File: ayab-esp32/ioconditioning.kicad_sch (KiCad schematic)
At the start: 41 parts, among them U702 LM393, U703 LM393

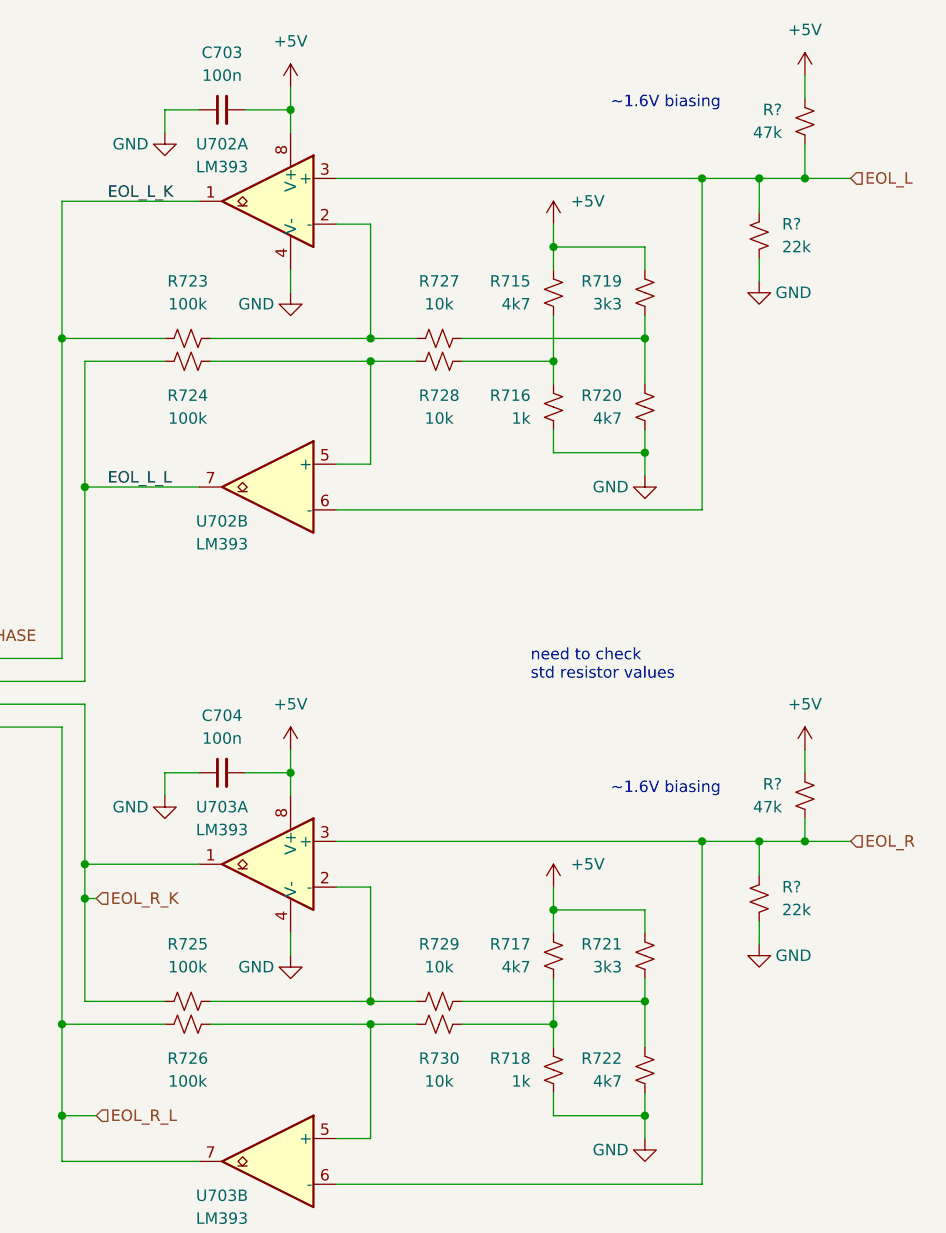
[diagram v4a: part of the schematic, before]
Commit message: refactor for i2c expander
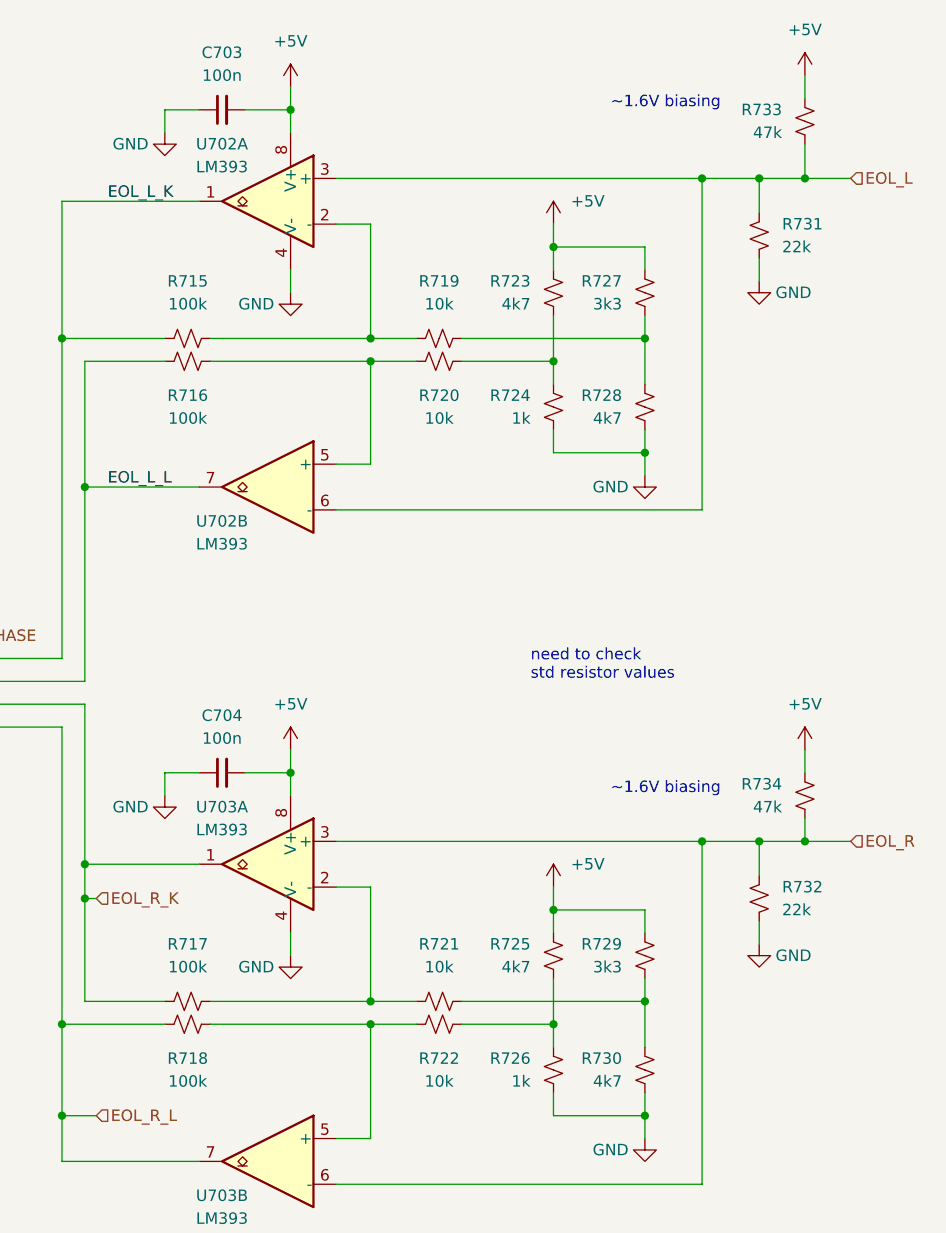
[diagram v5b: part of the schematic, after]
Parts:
- gave numbers to parts that had none: 4
- renumbered R723 to R715, R724 to R716, R725 to R717, R726 to R718, R727 to R719, R728 to R720, R729 to R721, R730 to R722, R715 to R723, R716 to R724, R717 to R725, R718 to R726, R719 to R727, R720 to R728, R721 to R729, R722 to R730

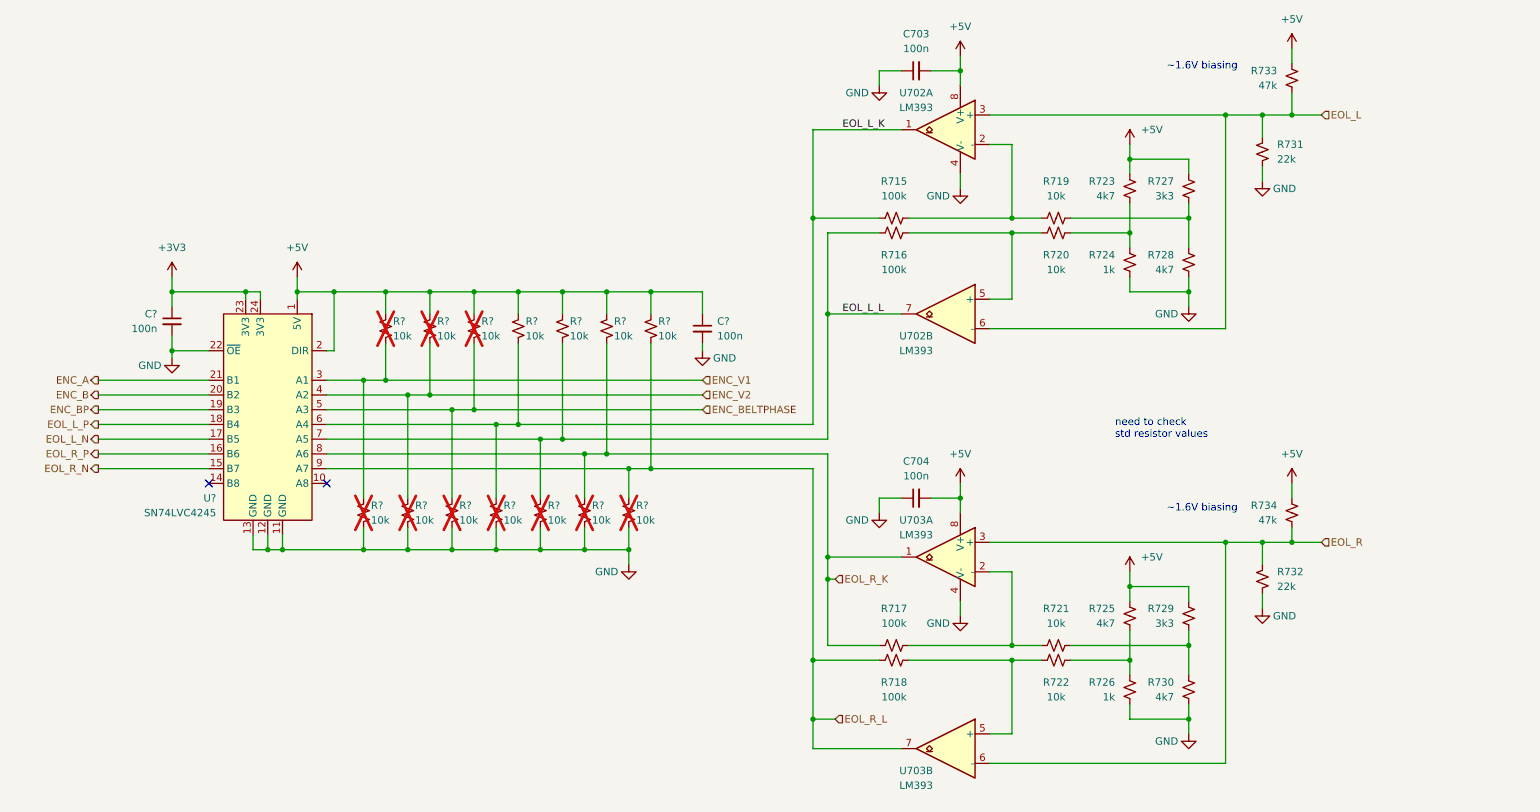
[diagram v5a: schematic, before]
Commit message: add component selection, bom
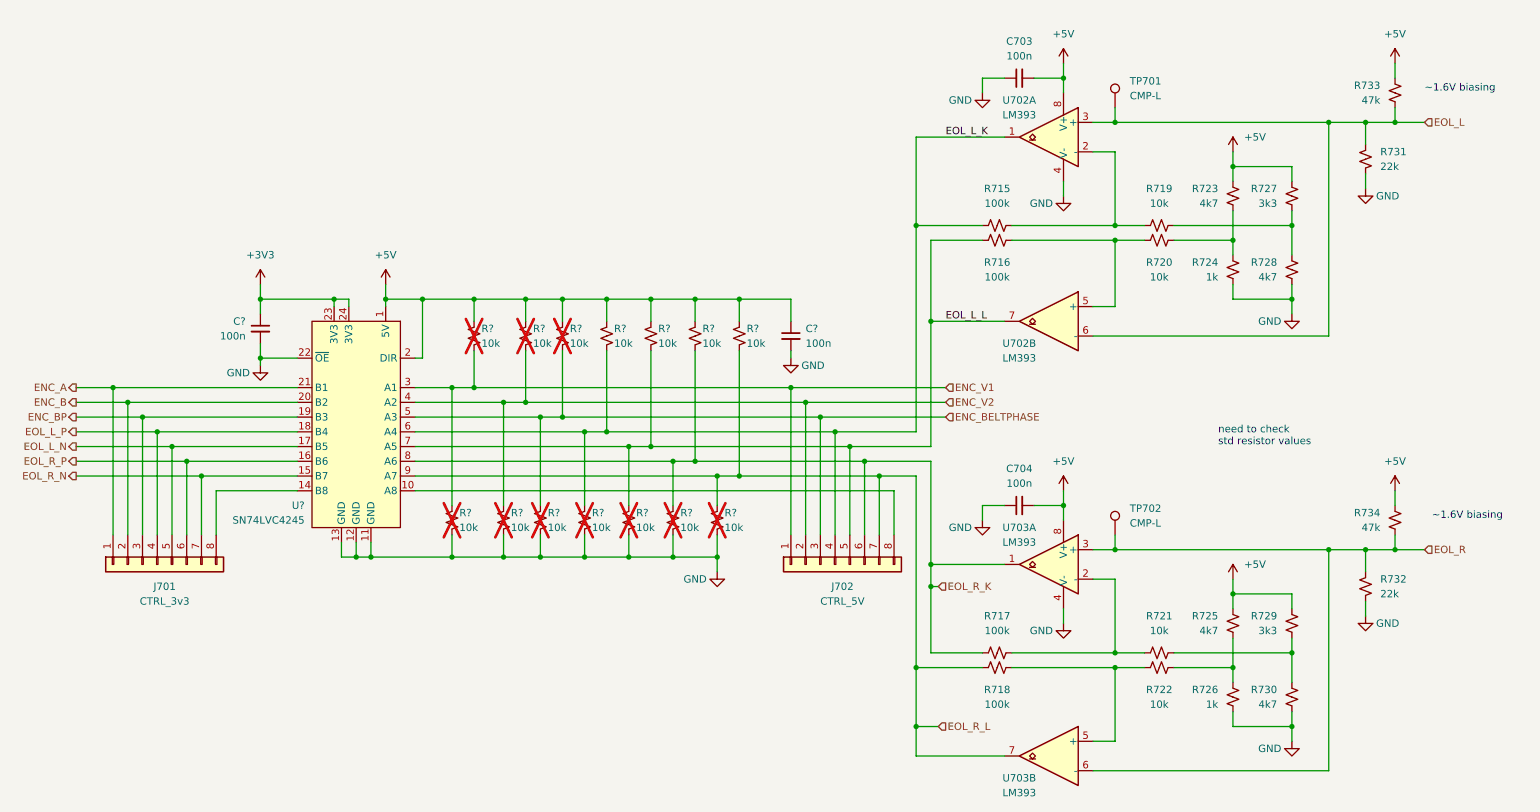
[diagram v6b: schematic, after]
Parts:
- added J701: CTRL_3v3, Connector_PinSocket_2.54mm:PinSocket_2x04_P2.54mm_Vertical, symbol Library:Conn_01x08
- added J702: CTRL_5V, Connector_PinSocket_2.54mm:PinSocket_2x04_P2.54mm_Vertical, symbol Library:Conn_01x08
- added TP701, TP702: CMP-L, TestPoint:TestPoint_Pad_D2.0mm, symbol Library:TestPoint
- C703, C704, C? (x2): footprint (none) -> Capacitor_SMD:C_0603_1608Metric; symbol ayab-esp32:C_Small -> Library:C_Small; LCSC ID (none) -> C57112; OEM (none) -> FH (Guangdong Fenghua Advanced Tech); OEM PN (none) -> 0603B103K500NT; Package (none) -> 0603; Voltage rating (none) -> 24V X7R
- R715, R716, R717, R718: footprint (none) -> Resistor_SMD:R_0603_1608Metric; symbol ayab-esp32:R_Small_US -> Library:R_Small_US; LCSC ID (none) -> C25803; OEM (none) -> UNI-ROYAL(Uniroyal Elec); OEM PN (none) -> 0603WAF1003T5E; Package (none) -> 0603
- R719, R720, R721, R722, R? (x14): footprint (none) -> Resistor_SMD:R_0603_1608Metric; symbol ayab-esp32:R_Small_US -> Library:R_Small_US; LCSC ID (none) -> C25804; OEM (none) -> UNI-ROYAL(Uniroyal Elec); OEM PN (none) -> 0603WAF1002T5E; Package (none) -> 0603
- R723, R725, R728, R730: footprint (none) -> Resistor_SMD:R_0603_1608Metric; symbol ayab-esp32:R_Small_US -> Library:R_Small_US; LCSC ID (none) -> C23162; OEM (none) -> UNI-ROYAL(Uniroyal Elec); OEM PN (none) -> 0603WAF4701T5E; Package (none) -> 0603
- R724, R726: footprint (none) -> Resistor_SMD:R_0603_1608Metric; symbol ayab-esp32:R_Small_US -> Library:R_Small_US; LCSC ID (none) -> C21190; OEM (none) -> UNI-ROYAL(Uniroyal Elec); OEM PN (none) -> 0603WAF1001T5E; Package (none) -> 0603
- R727, R729: footprint (none) -> Resistor_SMD:R_0603_1608Metric; symbol ayab-esp32:R_Small_US -> Library:R_Small_US; LCSC ID (none) -> C22978; OEM (none) -> UNI-ROYAL(Uniroyal Elec); OEM PN (none) -> 0603WAF3301T5E; Package (none) -> 0603
- R731, R732: footprint (none) -> Resistor_SMD:R_0603_1608Metric; symbol ayab-esp32:R_Small_US -> Library:R_Small_US; LCSC ID (none) -> C31850; OEM (none) -> UNI-ROYAL(Uniroyal Elec); OEM PN (none) -> 0603WAF2202T5E; Package (none) -> 0603
- R733, R734: footprint (none) -> Resistor_SMD:R_0603_1608Metric; symbol ayab-esp32:R_Small_US -> Library:R_Small_US; LCSC ID (none) -> C25819; OEM (none) -> UNI-ROYAL(Uniroyal Elec); OEM PN (none) -> 0603WAF4702T5E; Package (none) -> 0603
- U702, U703: footprint (none) -> Package_SO:SOIC-8_3.9x4.9mm_P1.27mm; symbol ayab-esp32:LM393 -> Library:LM393; OEM (none) -> onsemi; OEM PN (none) -> LM393DR2G; Package (none) -> SOIC-8
- U?: symbol ayab-esp32:SN74LVC4245A -> Library:SN74LVC4245A; LCSC ID (none) -> C7859; OEM (none) -> Texas Instruments; OEM PN (none) -> SN74LVC4245APWR; Package (none) -> TSSOP-24
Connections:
- net ENC_A: now also J701.1 (Pin_1)
- net ENC_B: now also J701.2 (Pin_2)
- net ENC_BELTPHASE: now also J702.3 (Pin_3)
- net ENC_BP: now also J701.3 (Pin_3)
- net ENC_V1: now also J702.1 (Pin_1)
- net ENC_V2: now also J702.2 (Pin_2)
- net EOL_L: now also TP701.1
- net EOL_L_K: now also J702.4 (Pin_4)
- net EOL_L_L: now also J702.5 (Pin_5)
- net EOL_L_N: now also J701.5 (Pin_5)
- net EOL_L_P: now also J701.4 (Pin_4)
- net EOL_R: now also TP702.1
- net EOL_R_K: now also J702.6 (Pin_6)
- net EOL_R_L: now also J702.7 (Pin_7)
- net EOL_R_N: now also J701.7 (Pin_7)
- net EOL_R_P: now also J701.6 (Pin_6)
- net at U?.10 (A8): now also J702.8 (Pin_8)
- net at U?.14 (B8): now also J701.8 (Pin_8)
- no-connect marks 2 -> 0
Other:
- moved on the sheet: C703, C704, C?, R715, R716, R717, R718, R719, R720, R721, R722, R723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

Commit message: review ZVD P-ch MOSFET and resistors
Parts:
- C703, C704, C? (x2): symbol Library:C_Small -> ayab-lib:C_Small
- J701, J702: symbol Library:Conn_01x08 -> ayab-lib:Conn_01x08
- R715, R716, R717, R718, R719, R720, R721, R722, R723, R724, R725, R726, R727, R728, R729, R730, R731, R732, R733, R734, R? (x14): symbol Library:R_Small_US -> ayab-lib:R_Small_US
- TP701, TP702: symbol Library:TestPoint -> ayab-lib:TestPoint
- U702, U703: symbol Library:LM393 -> ayab-lib:LM393
- U?: symbol Library:SN74LVC4245A -> ayab-lib:SN74LVC4245A

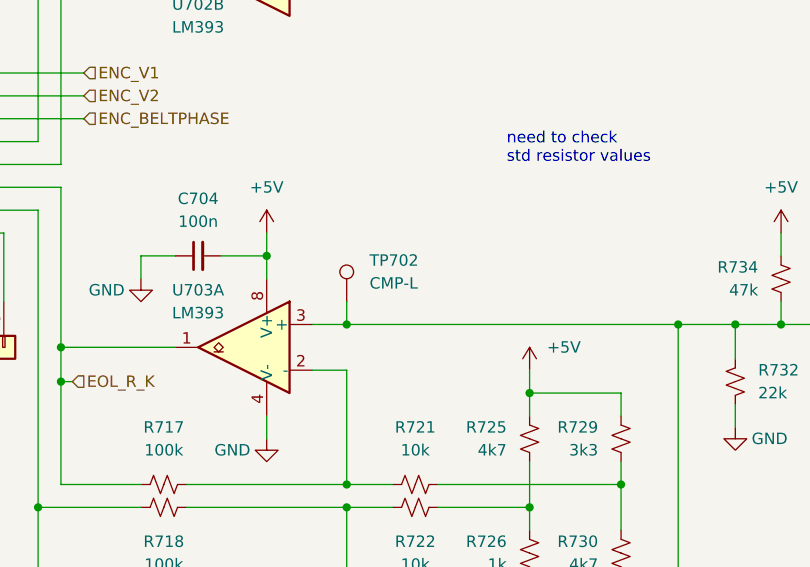
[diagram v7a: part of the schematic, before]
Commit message: first draft layout DRC clean
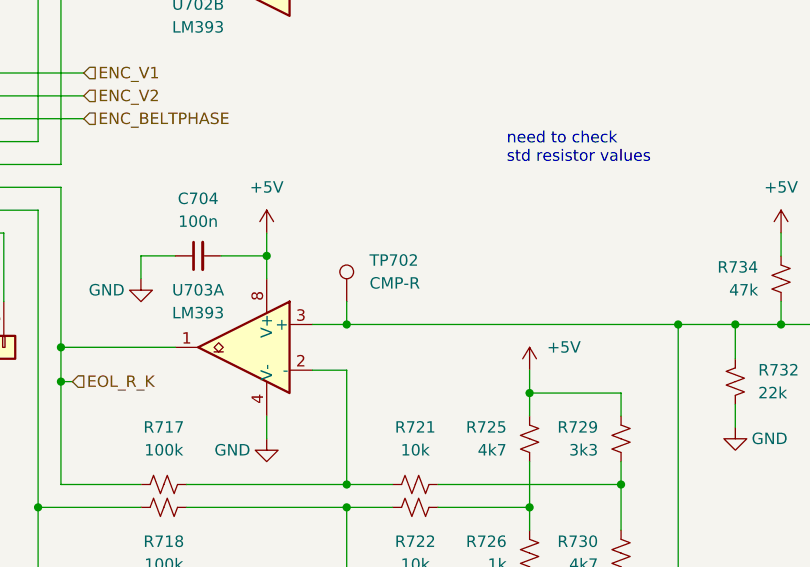
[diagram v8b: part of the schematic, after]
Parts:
- J701, J702: footprint Connector_PinSocket_2.54mm:PinSocket_2x04_P2.54mm_Vertical -> Connector_PinHeader_2.54mm:PinHeader_2x04_P2.54mm_Vertical
- TP701: footprint TestPoint:TestPoint_Pad_D2.0mm -> TestPoint:TestPoint_Pad_D1.0mm
- TP702: value CMP-L -> CMP-R; footprint TestPoint:TestPoint_Pad_D2.0mm -> TestPoint:TestPoint_Pad_D1.0mm
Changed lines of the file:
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@@
       (effects (font (size 1.27 1.27)) (justify left))
     )
-    (property "Footprint" "TestPoint:TestPoint_Pad_D2.0mm" (at 218.44 38.1 0)
+    (property "Footprint" "TestPoint:TestPoint_Pad_D1.0mm" (at 218.44 38.1 0)
       (effects (font (size 1.27 1.27)) hide)
     )
@@
       (effects (font (size 1.27 1.27)))
     )
-    (property "Footprint" "Connector_PinSocket_2.54mm:PinSocket_2x04_P2.54mm_Vertical" (at 48.26 116.84 0)
+    (property "Footprint" "Connector_PinHeader_2.54mm:PinHeader_2x04_P2.54mm_Vertical" (at 48.26 116.84 0)
       (effects (font (size 1.27 1.27)) hide)
     )
@@
       (effects (font (size 1.27 1.27)))
     )
-    (property "Footprint" "Connector_PinSocket_2.54mm:PinSocket_2x04_P2.54mm_Vertical" (at 165.1 116.84 0)
+    (property "Footprint" "Connector_PinHeader_2.54mm:PinHeader_2x04_P2.54mm_Vertical" (at 165.1 116.84 0)
       (effects (font (size 1.27 1.27)) hide)
     )
@@
       (effects (font (size 1.27 1.27)) (justify left))
     )
-    (property "Value" "CMP-L" (at 215.9 109.728 0)
+    (property "Value" "CMP-R" (at 215.9 109.728 0)
       (effects (font (size 1.27 1.27)) (justify left))
     )
-    (property "Footprint" "TestPoint:TestPoint_Pad_D2.0mm" (at 218.44 111.76 0)
-      (effects (font (size 1.27 1.27)) hide)
-    )
+    (property "Footprint" "TestPoint:TestPoint_Pad_D1.0mm" (at 218.44 111.76 0)
+      (effects (font (size 1.27 1.27)) hide)
+    )
